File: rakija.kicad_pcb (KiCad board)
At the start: 2 copper layers, 34 x 59.8 mm, 0 parts

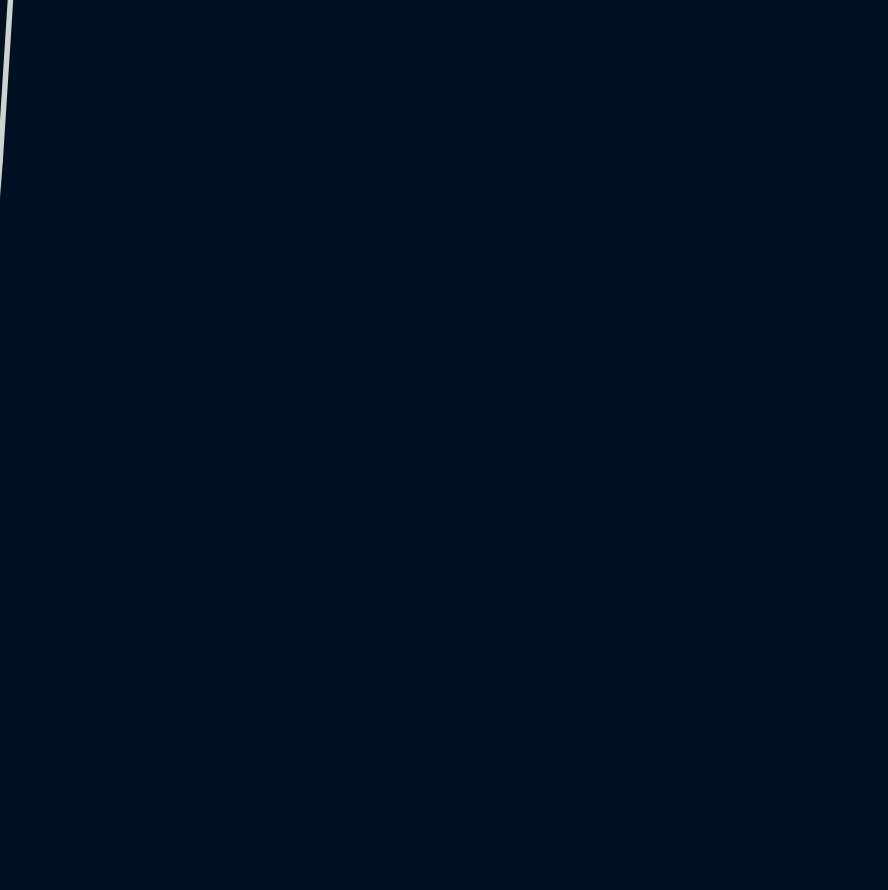
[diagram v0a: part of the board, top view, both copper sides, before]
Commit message: added some components
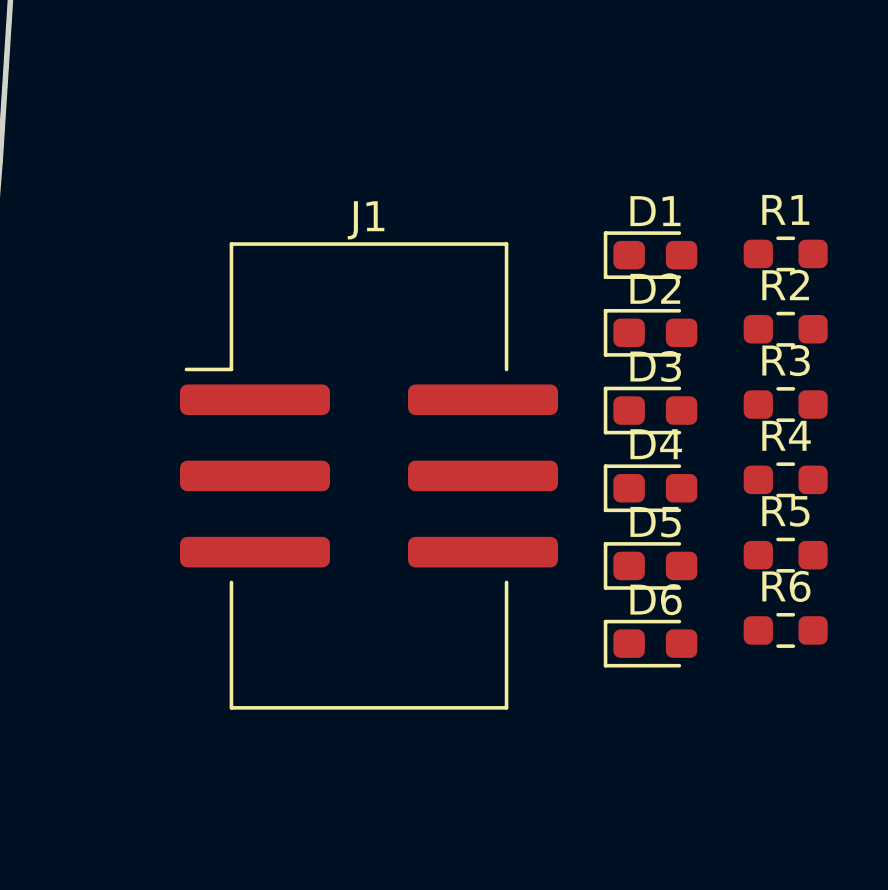
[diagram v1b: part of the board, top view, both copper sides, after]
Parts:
- added D1: LED, LED_SMD:LED_0603_1608Metric_Pad1.05x0.95mm_HandSolder, F.Cu at (182.9, 92.8)
- added D2: LED, LED_SMD:LED_0603_1608Metric_Pad1.05x0.95mm_HandSolder, F.Cu at (182.9, 95.4)
- added D3: LED, LED_SMD:LED_0603_1608Metric_Pad1.05x0.95mm_HandSolder, F.Cu at (182.9, 98.0)
- added D4: LED, LED_SMD:LED_0603_1608Metric_Pad1.05x0.95mm_HandSolder, F.Cu at (182.9, 100.6)
- added D5: LED, LED_SMD:LED_0603_1608Metric_Pad1.05x0.95mm_HandSolder, F.Cu at (182.9, 103.2)
- added D6: LED, LED_SMD:LED_0603_1608Metric_Pad1.05x0.95mm_HandSolder, F.Cu at (182.9, 105.7)
- added J1: Conn_02x03_Odd_Even, Connector_IDC:IDC-Header_2x03_P2.54mm_Vertical_SMD, F.Cu at (173.3, 100.2)
- added R1: TBD, Resistor_SMD:R_0603_1608Metric_Pad0.98x0.95mm_HandSolder, F.Cu at (187.2, 92.8)
- added R2: TBD, Resistor_SMD:R_0603_1608Metric_Pad0.98x0.95mm_HandSolder, F.Cu at (187.2, 95.3)
- added R3: TBD, Resistor_SMD:R_0603_1608Metric_Pad0.98x0.95mm_HandSolder, F.Cu at (187.2, 97.8)
- added R4: TBD, Resistor_SMD:R_0603_1608Metric_Pad0.98x0.95mm_HandSolder, F.Cu at (187.2, 100.3)
- added R5: TBD, Resistor_SMD:R_0603_1608Metric_Pad0.98x0.95mm_HandSolder, F.Cu at (187.2, 102.8)
- added R6: TBD, Resistor_SMD:R_0603_1608Metric_Pad0.98x0.95mm_HandSolder, F.Cu at (187.2, 105.3)

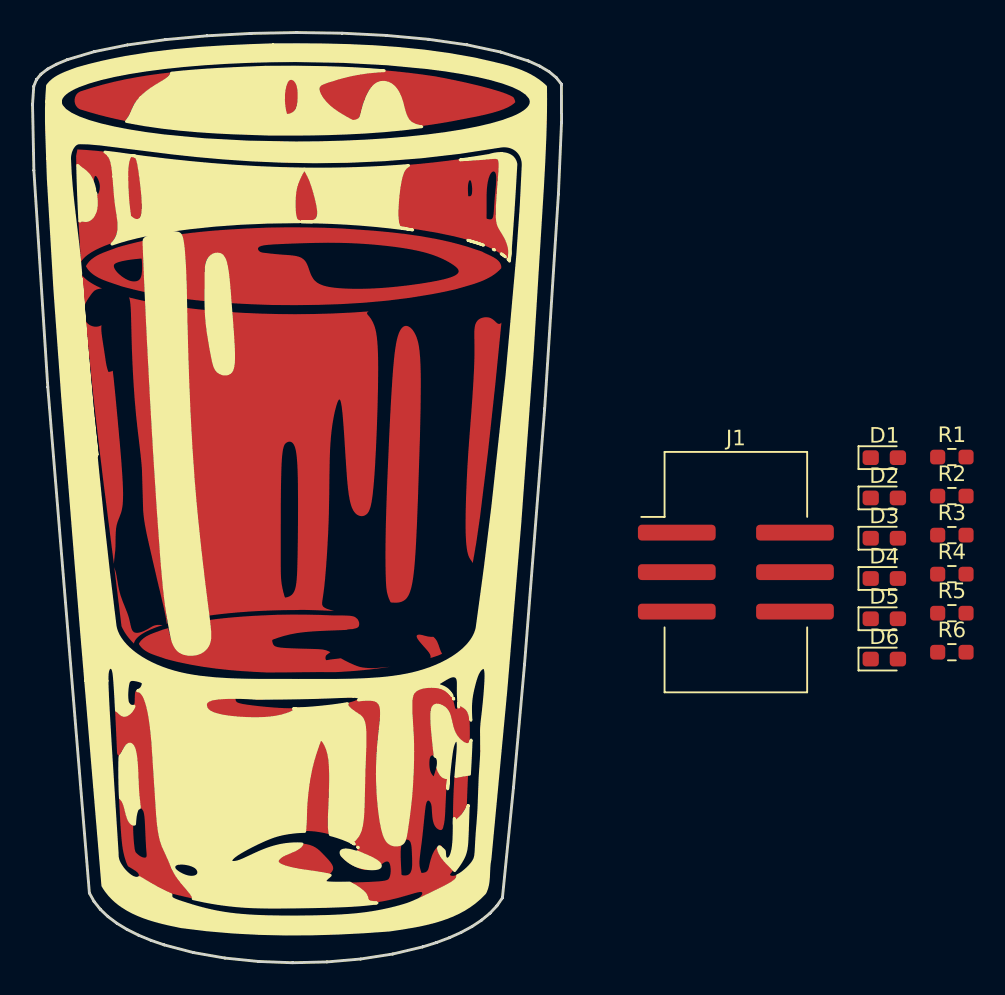
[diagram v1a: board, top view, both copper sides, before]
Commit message: leds routed
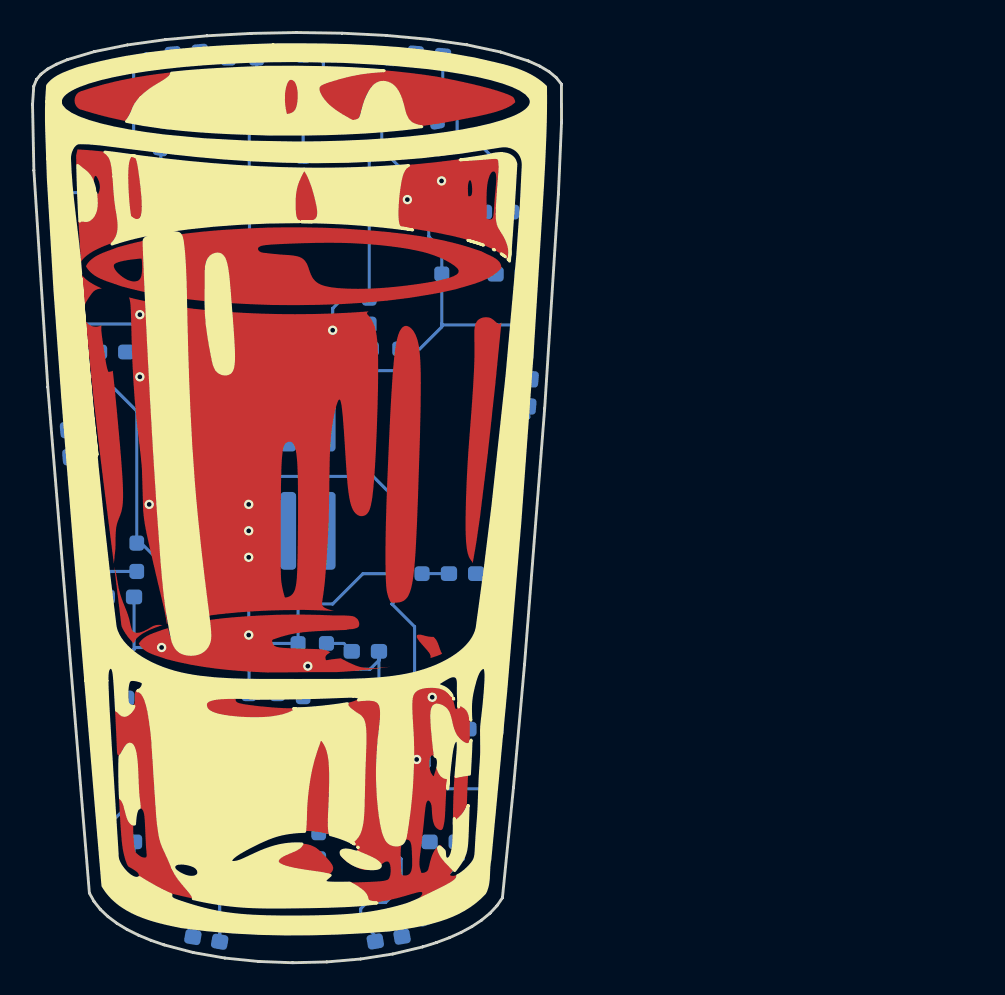
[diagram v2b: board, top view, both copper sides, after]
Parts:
- added D10: LED, LED_SMD:LED_0603_1608Metric_Pad1.05x0.95mm_HandSolder, B.Cu at (135.0, 108.2)
- added D11: LED, LED_SMD:LED_0603_1608Metric_Pad1.05x0.95mm_HandSolder, B.Cu at (133.2, 86.0)
- added D12: LED, LED_SMD:LED_0603_1608Metric_Pad1.05x0.95mm_HandSolder, B.Cu at (160.1, 88.6)
- added D13: LED, LED_SMD:LED_0603_1608Metric_Pad1.05x0.95mm_HandSolder, B.Cu at (130.4, 91.9)
- added D14: LED, LED_SMD:LED_0603_1608Metric_Pad1.05x0.95mm_HandSolder, B.Cu at (133.8, 101.8)
- added D15: LED, LED_SMD:LED_0603_1608Metric_Pad1.05x0.95mm_HandSolder, B.Cu at (132.5, 75.8)
- added D16: LED, LED_SMD:LED_0603_1608Metric_Pad1.05x0.95mm_HandSolder, B.Cu at (158.8, 81.0)
- added D17: LED, LED_SMD:LED_0603_1608Metric_Pad1.05x0.95mm_HandSolder, B.Cu at (155.8, 100.2)
- added D18: LED, LED_SMD:LED_0603_1608Metric_Pad1.05x0.95mm_HandSolder, B.Cu at (149.5, 105.2)
- added D19: LED, LED_SMD:LED_0603_1608Metric_Pad1.05x0.95mm_HandSolder, B.Cu at (157.0, 110.2)
- added D20: LED, LED_SMD:LED_0603_1608Metric_Pad1.05x0.95mm_HandSolder, B.Cu at (154.5, 117.5)
- added D21: LED, LED_SMD:LED_0603_1608Metric_Pad1.05x0.95mm_HandSolder, B.Cu at (135.5, 117.5)
- added D22: LED, LED_SMD:LED_0603_1608Metric_Pad1.05x0.95mm_HandSolder, B.Cu at (151.0, 123.8)
- added D23: LED, LED_SMD:LED_0603_1608Metric_Pad1.05x0.95mm_HandSolder, B.Cu at (139.3, 123.8)
- added D24: LED, LED_SMD:LED_0603_1608Metric_Pad1.05x0.95mm_HandSolder, B.Cu at (146.5, 117.8)
- added D7: LED, LED_SMD:LED_0603_1608Metric_Pad1.05x0.95mm_HandSolder, B.Cu at (158.0, 77.0)
- added D8: LED, LED_SMD:LED_0603_1608Metric_Pad1.05x0.95mm_HandSolder, B.Cu at (149.8, 83.4)
- added D9: LED, LED_SMD:LED_0603_1608Metric_Pad1.05x0.95mm_HandSolder, B.Cu at (145.5, 109.0)
- added R10: TBD, Resistor_SMD:R_0603_1608Metric_Pad0.98x0.95mm_HandSolder, B.Cu at (135.9, 110.8)
- added R11: TBD, Resistor_SMD:R_0603_1608Metric_Pad0.98x0.95mm_HandSolder, B.Cu at (130.8, 85.1)
- added R12: TBD, Resistor_SMD:R_0603_1608Metric_Pad0.98x0.95mm_HandSolder, B.Cu at (159.8, 85.2)
- added R13: TBD, Resistor_SMD:R_0603_1608Metric_Pad0.98x0.95mm_HandSolder, B.Cu at (131.0, 88.5)
- added R14: TBD, Resistor_SMD:R_0603_1608Metric_Pad0.98x0.95mm_HandSolder, B.Cu at (134.8, 99.2)
- added R15: TBD, Resistor_SMD:R_0603_1608Metric_Pad0.98x0.95mm_HandSolder, B.Cu at (130.1, 76.2)
- added R16: TBD, Resistor_SMD:R_0603_1608Metric_Pad0.98x0.95mm_HandSolder, B.Cu at (155.3, 81.0)
- added R17: TBD, Resistor_SMD:R_0603_1608Metric_Pad0.98x0.95mm_HandSolder, B.Cu at (152.2, 100.3)
- added R18: TBD, Resistor_SMD:R_0603_1608Metric_Pad0.98x0.95mm_HandSolder, B.Cu at (146.1, 104.7)
- added R19: TBD, Resistor_SMD:R_0603_1608Metric_Pad0.98x0.95mm_HandSolder, B.Cu at (153.6, 110.2)
- added R20: TBD, Resistor_SMD:R_0603_1608Metric_Pad0.98x0.95mm_HandSolder, B.Cu at (152.5, 115.0)
- added R21: TBD, Resistor_SMD:R_0603_1608Metric_Pad0.98x0.95mm_HandSolder, B.Cu at (138.0, 116.5)
- added R22: TBD, Resistor_SMD:R_0603_1608Metric_Pad0.98x0.95mm_HandSolder, B.Cu at (154.2, 122.1)
- added R23: TBD, Resistor_SMD:R_0603_1608Metric_Pad0.98x0.95mm_HandSolder, B.Cu at (136.1, 122.0)
- added R24: TBD, Resistor_SMD:R_0603_1608Metric_Pad0.98x0.95mm_HandSolder, B.Cu at (145.3, 120.2)
- added R7: TBD, Resistor_SMD:R_0603_1608Metric_Pad0.98x0.95mm_HandSolder, B.Cu at (154.5, 77.0)
- added R8: TBD, Resistor_SMD:R_0603_1608Metric_Pad0.98x0.95mm_HandSolder, B.Cu at (150.8, 85.8)
- added R9: TBD, Resistor_SMD:R_0603_1608Metric_Pad0.98x0.95mm_HandSolder, B.Cu at (142.9, 108.0)
- D1, D2, D3, D4, D5, D6, J1, R1, R2, R3, R4, R5, R6: moved to B.Cu
- moved R6 60.9 mm to (138.0, 69.4), turned to 180 degrees
- moved D6 57.3 mm to (136.5, 72.0), turned to 80 degrees
- moved R2 53.6 mm to (141.6, 67.1), turned to 180 degrees
- moved D2 53.2 mm to (138.0, 66.8), turned to 5 degrees
- moved R3 52.8 mm to (142.9, 68.9)
- moved R4 50.8 mm to (143.0, 75.4)
- moved D3 48.1 mm to (145.5, 67.8), turned to -90 degrees
- moved R5 47.8 mm to (151.5, 71.0)
- moved D4 45.7 mm to (145.5, 74.2), turned to -90 degrees
- moved R1 43.8 mm to (151.0, 68.0), turned to 85 degrees
- moved D5 42.3 mm to (154.2, 72.0), turned to 100 degrees
- moved D1 39.1 mm to (153.6, 66.9), turned to 175 degrees
- moved J1 29.5 mm to (144.5, 93.7), turned to -90 degrees
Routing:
- net GND: track 0.00 -> 211.7 mm, vias 0 -> 14
- net +3V0: track 0.00 -> 209.8 mm
- net Net-(D14-A): track 0.00 -> 3.44 mm
- net Net-(D20-A): track 0.00 -> 2.48 mm
- net Net-(D22-A): track 0.00 -> 2.47 mm
- net Net-(D23-A): track 0.00 -> 2.44 mm
- net Net-(D2-A): track 0.00 -> 1.99 mm
- net Net-(D6-A): track 0.00 -> 1.96 mm
- net Net-(D13-A): track 0.00 -> 1.86 mm
- net Net-(D18-A): track 0.00 -> 1.84 mm
- net Net-(D12-A): track 0.00 -> 1.79 mm
- net Net-(D5-A): track 0.00 -> 1.78 mm
- net Net-(D1-A): track 0.00 -> 1.78 mm
- net Net-(D3-A): track 0.00 -> 1.76 mm
- net Net-(D17-A): track 0.00 -> 1.73 mm
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
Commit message: ready for gerber
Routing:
- net +3V0: track 209.8 -> 214.5 mm
- net GND: track 211.7 -> 212.3 mm
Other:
- board text added: "(drink responsibly)"
- board text added: "@borisnotes"
- board text added: "GND"
- board text added: "VCC"
- board text added: "Живели!"
